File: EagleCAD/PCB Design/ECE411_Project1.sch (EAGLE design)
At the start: 23 parts

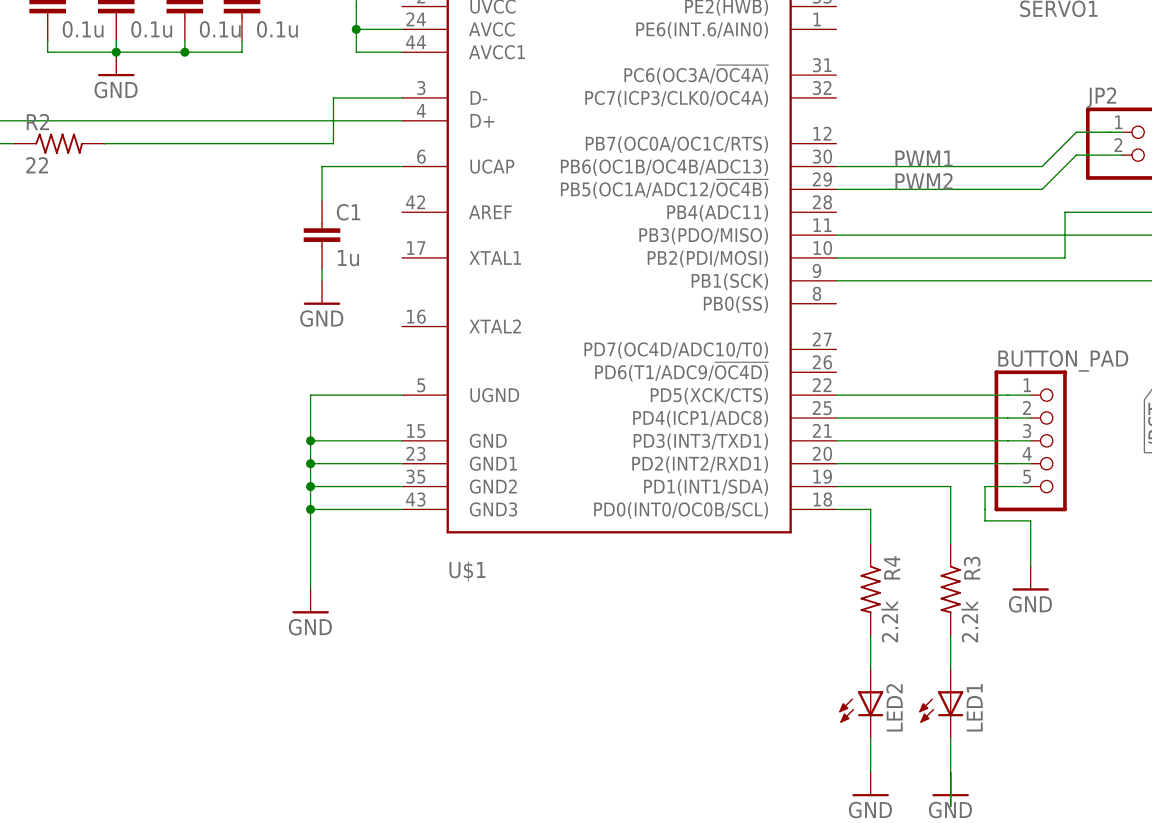
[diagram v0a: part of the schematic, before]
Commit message: Made Xtal library file
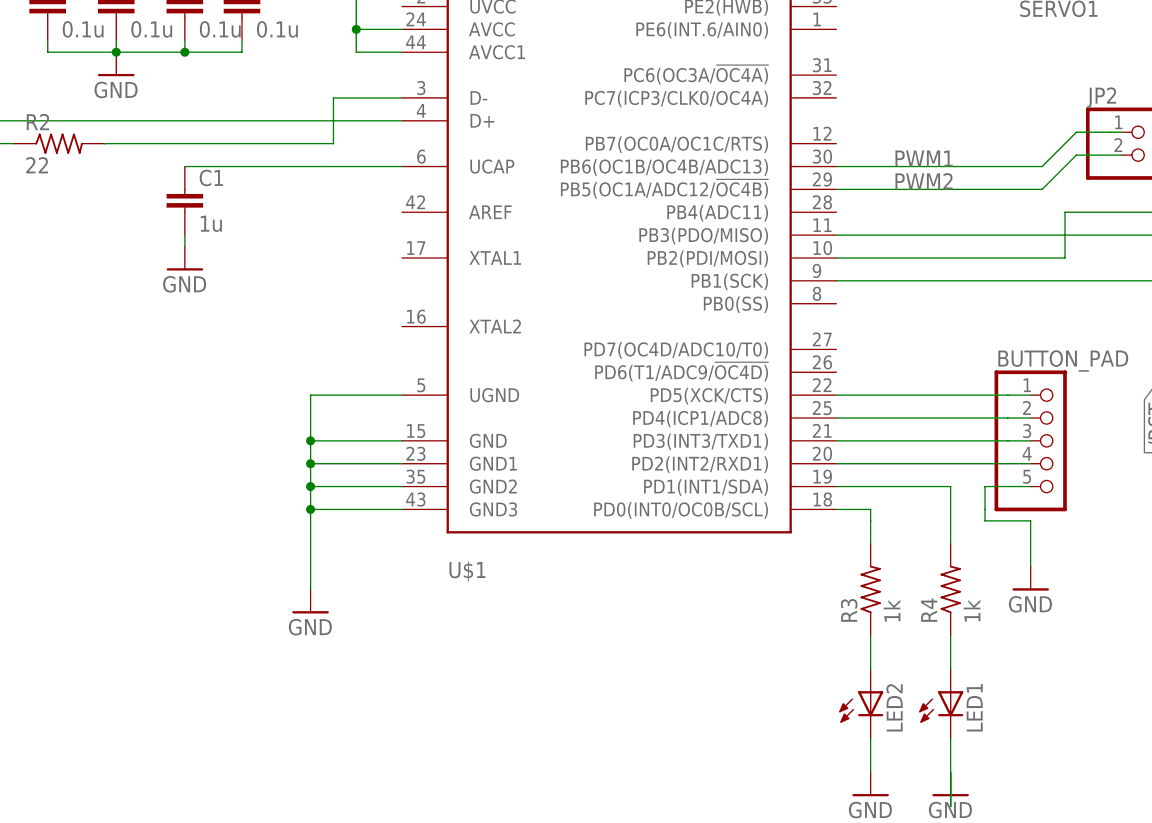
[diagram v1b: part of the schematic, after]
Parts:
- LED1, LED2: device adafruit:LED -> led:LEDSMT1206
- R3, R4: value (none) -> 1k; device rcl:R-US_0204/2V -> rcl:R-US_R1206; SPICEPREFIX 2.2k -> (none)
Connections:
- net N$10: now also R4.1; no longer R3.2
- net N$6: now also R3.2; no longer R4.1
- net N$8: now also R4.2; no longer R3.1
- net N$9: now also R3.1; no longer R4.2
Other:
- moved on the sheet: C1, R3, R4
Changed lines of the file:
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@@
 <part name="+3V1" library="supply1" library_urn="urn:adsk.eagle:library:371" deviceset="+3V3" device=""/>
 <part name="GND2" library="supply1" library_urn="urn:adsk.eagle:library:371" deviceset="GND" device=""/>
-<part name="LED1" library="adafruit" deviceset="LED" device=""/>
-<part name="R3" library="rcl" library_urn="urn:adsk.eagle:library:334" deviceset="R-US_" device="0204/2V" package3d_urn="urn:adsk.eagle:package:23495/1">
-<spice>
-<pinmapping spiceprefix="R">
-<pinmap gate="G$1" pin="1" pinorder="1"/>
-<pinmap gate="G$1" pin="2" pinorder="2"/>
-</pinmapping>
-</spice>
-<attribute name="SPICEPREFIX" value="2.2k"/>
-</part>
-<part name="R4" library="rcl" library_urn="urn:adsk.eagle:library:334" deviceset="R-US_" device="0204/2V" package3d_urn="urn:adsk.eagle:package:23495/1">
-<spice>
-<pinmapping spiceprefix="R">
-<pinmap gate="G$1" pin="1" pinorder="1"/>
-<pinmap gate="G$1" pin="2" pinorder="2"/>
-</pinmapping>
-</spice>
-<attribute name="SPICEPREFIX" value="2.2k"/>
-</part>
-<part name="LED2" library="adafruit" deviceset="LED" device=""/>
 <part name="GND3" library="supply1" library_urn="urn:adsk.eagle:library:371" deviceset="GND" device=""/>
 <part name="GND4" library="supply1" library_urn="urn:adsk.eagle:library:371" deviceset="GND" device=""/>
@@
 <part name="C1" library="rcl" library_urn="urn:adsk.eagle:library:334" deviceset="C-EU" device="C1206" package3d_urn="urn:adsk.eagle:package:23618/2" value="1u"/>
 <part name="R5" library="rcl" library_urn="urn:adsk.eagle:library:334" deviceset="R-US_" device="R1206" package3d_urn="urn:adsk.eagle:package:23540/2" value="10k"/>
+<part name="R3" library="rcl" library_urn="urn:adsk.eagle:library:334" deviceset="R-US_" device="R1206" package3d_urn="urn:adsk.eagle:package:23540/2" value="1k"/>
+<part name="R4" library="rcl" library_urn="urn:adsk.eagle:library:334" deviceset="R-US_" device="R1206" package3d_urn="urn:adsk.eagle:package:23540/2" value="1k"/>
+<part name="LED2" library="led" library_urn="urn:adsk.eagle:library:259" deviceset="LED" device="SMT1206" package3d_urn="urn:adsk.eagle:package:15796/1"/>
+<part name="LED1" library="led" library_urn="urn:adsk.eagle:library:259" deviceset="LED" device="SMT1206" package3d_urn="urn:adsk.eagle:package:15796/1"/>
 </parts>
 <sheets>
@@
 <instance part="MICRO_USB_TYPE_B" gate="G$1" x="-96.52" y="50.8"/>
 <instance part="+3V1" gate="G$1" x="-60.96" y="83.82"/>
-<instance part="GND2" gate="1" x="-30.48" y="33.02"/>
-<instance part="LED1" gate="G$1" x="39.37" y="-10.16">
-<attribute name="VALUE" x="45.085" y="-14.732" size="1.778" layer="96" rot="R90"/>
-</instance>
-<instance part="R3" gate="G$1" x="39.37" y="1.27" rot="R270">
-<attribute name="VALUE" x="36.068" y="5.08" size="1.778" layer="96" rot="R270"/>
-<attribute name="SPICEPREFIX" x="40.64" y="0" size="1.778" layer="96" rot="R270"/>
-</instance>
-<instance part="R4" gate="G$1" x="30.48" y="1.27" rot="R270">
-<attribute name="VALUE" x="27.178" y="5.08" size="1.778" layer="96" rot="R270"/>
-<attribute name="SPICEPREFIX" x="31.75" y="0" size="1.778" layer="96" rot="R270"/>
-</instance>
-<instance part="LED2" gate="G$1" x="30.48" y="-10.16">
-<attribute name="VALUE" x="36.195" y="-14.732" size="1.778" layer="96" rot="R90"/>
-</instance>
+<instance part="GND2" gate="1" x="-45.72" y="36.83"/>
 <instance part="GND3" gate="1" x="30.48" y="-21.59"/>
 <instance part="GND4" gate="1" x="39.37" y="-21.59"/>
@@
 <instance part="R1" gate="G$1" x="-72.39" y="53.34"/>
 <instance part="R2" gate="G$1" x="-59.69" y="50.8"/>
-<instance part="C1" gate="G$1" x="-30.48" y="41.91"/>
+<instance part="C1" gate="G$1" x="-45.72" y="45.72"/>
 <instance part="R5" gate="G$1" x="-27.94" y="92.71" rot="R90"/>
+<instance part="R3" gate="G$1" x="30.48" y="1.27" rot="R90"/>
+<instance part="R4" gate="G$1" x="39.37" y="1.27" rot="R90"/>
+<instance part="LED2" gate="G$1" x="30.48" y="-10.16"/>
+<instance part="LED1" gate="G$1" x="39.37" y="-10.16"/>
 </instances>
 <busses>
@@
 <segment>
 <pinref part="GND2" gate="1" pin="GND"/>
-<wire x1="-30.48" y1="36.83" x2="-30.48" y2="35.56" width="0.1524" layer="91"/>
+<wire x1="-45.72" y1="40.64" x2="-45.72" y2="39.37" width="0.1524" layer="91"/>
 <pinref part="C1" gate="G$1" pin="2"/>
 </segment>
 <segment>
-<pinref part="LED2" gate="G$1" pin="C"/>
 <wire x1="30.48" y1="-15.24" x2="30.48" y2="-19.05" width="0.1524" layer="91"/>
 <pinref part="GND3" gate="1" pin="GND"/>
-</segment>
-<segment>
-<pinref part="LED1" gate="G$1" pin="C"/>
+<pinref part="LED2" gate="G$1" pin="C"/>
+</segment>
+<segment>
 <wire x1="39.37" y1="-15.24" x2="39.37" y2="-22.86" width="0.1524" layer="91"/>
 <wire x1="39.37" y1="-22.86" x2="39.37" y2="-19.05" width="0.1524" layer="91"/>
 <pinref part="GND4" gate="1" pin="GND"/>
+<pinref part="LED1" gate="G$1" pin="C"/>
 </segment>
 <segment>
@@
 <pinref part="U$1" gate="G$1" pin="UCAP"/>
 <wire x1="-21.59" y1="48.26" x2="-30.48" y2="48.26" width="0.1524" layer="91"/>
-<wire x1="-30.48" y1="48.26" x2="-30.48" y2="44.45" width="0.1524" layer="91"/>
+<wire x1="-30.48" y1="48.26" x2="-45.72" y2="48.26" width="0.1524" layer="91"/>
 <pinref part="C1" gate="G$1" pin="1"/>
 </segment>
@@
 <wire x1="26.67" y1="10.16" x2="30.48" y2="10.16" width="0.1524" layer="91"/>
 <wire x1="30.48" y1="10.16" x2="30.48" y2="8.89" width="0.1524" layer="91"/>
+<wire x1="30.48" y1="8.89" x2="30.48" y2="6.35" width="0.1524" layer="91"/>
+<pinref part="R3" gate="G$1" pin="2"/>
+</segment>
+</net>
+<net name="N$9" class="0">
+<segment>
+<wire x1="30.48" y1="-3.81" x2="30.48" y2="-7.62" width="0.1524" layer="91"/>
+<pinref part="R3" gate="G$1" pin="1"/>
+<pinref part="LED2" gate="G$1" pin="A"/>
+</segment>
+</net>
+<net name="N$10" class="0">
+<segment>
+<wire x1="39.37" y1="-3.81" x2="39.37" y2="-7.62" width="0.1524" layer="91"/>
 <pinref part="R4" gate="G$1" pin="1"/>
-<wire x1="30.48" y1="8.89" x2="30.48" y2="6.35" width="0.1524" layer="91"/>
-</segment>
-</net>
-<net name="N$9" class="0">
-<segment>
-<pinref part="R4" gate="G$1" pin="2"/>
-<pinref part="LED2" gate="G$1" pin="A"/>
-<wire x1="30.48" y1="-3.81" x2="30.48" y2="-7.62" width="0.1524" layer="91"/>
-</segment>
-</net>
-<net name="N$10" class="0">
-<segment>
-<pinref part="R3" gate="G$1" pin="2"/>
 <pinref part="LED1" gate="G$1" pin="A"/>
-<wire x1="39.37" y1="-3.81" x2="39.37" y2="-7.62" width="0.1524" layer="91"/>
 </segment>
 </net>
@@
 <net name="N$8" class="0">
 <segment>
-<pinref part="R3" gate="G$1" pin="1"/>
 <wire x1="39.37" y1="6.35" x2="39.37" y2="12.7" width="0.1524" layer="91"/>
 <pinref part="U$1" gate="G$1" pin="PD1(INT1/SDA)"/>
 <wire x1="39.37" y1="12.7" x2="26.67" y2="12.7" width="0.1524" layer="91"/>
-</segment>
-</net>
+<pinref part="R4" gate="G$1" pin="2"/>
+</segment>
+</net>

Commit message: updates to schematic
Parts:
- removed 5V1A_REGULATOR1, 5V1A_REGULATOR2: L7805ABV, L7805ABV:L7805ABV
- added 16MHZ: XTAL_ATS160SM-1, XTAL_ATS160SM-1:XTAL_ATS160SM-1
- added C6, C7: 12p, rcl:C-EUC1206
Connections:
- removed net +3V3: C2.1, C3.1, C4.1, C5.1, U$1.AVCC, U$1.AVCC1, U$1.VCC, U$1.VCC1
- new net N$20: 16MHZ.2, C7.2, U$1.XTAL2
- new net N$21: 16MHZ.1, C6.2, U$1.XTAL1
- net GND: now also C2.1, C3.1, C4.1, C5.1, C6.1, C7.1; no longer 5V1A_REGULATOR1.GND, 5V1A_REGULATOR2.GND, C2.2, C3.2, C4.2, C5.2
- net N$14: no longer 5V1A_REGULATOR1.VOUT
- net N$19: no longer 5V1A_REGULATOR2.VOUT
- net VCC: now also C2.2, C3.2, C4.2, C5.2, U$1.AVCC, U$1.AVCC1, U$1.VCC, U$1.VCC1
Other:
- moved on the sheet: C2, C3, C4, C5

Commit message: Added some custom library components, updated schematic with new xtal cap values, and updated links document
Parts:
- removed JP2: (no value), pinhead:PINHD-1X2
- C6, C7: value 12p -> 22p
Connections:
- net PWM1: now also SERVO1.1; no longer JP2.1
- net PWM2: now also SERVO2.1; no longer JP2.2
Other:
- moved on the sheet: SERVO1, SERVO2
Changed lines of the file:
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@@
 <part name="BUTTON_PAD" library="pinhead" library_urn="urn:adsk.eagle:library:325" deviceset="PINHD-1X5" device="" package3d_urn="urn:adsk.eagle:package:22469/2"/>
 <part name="GND11" library="supply1" library_urn="urn:adsk.eagle:library:371" deviceset="GND" device=""/>
-<part name="JP2" library="pinhead" library_urn="urn:adsk.eagle:library:325" deviceset="PINHD-1X2" device="" package3d_urn="urn:adsk.eagle:package:22435/2"/>
 <part name="GND12" library="supply1" library_urn="urn:adsk.eagle:library:371" deviceset="GND" device=""/>
 <part name="GND13" library="supply1" library_urn="urn:adsk.eagle:library:371" deviceset="GND" device=""/>
@@
 <part name="LED2" library="led" library_urn="urn:adsk.eagle:library:259" deviceset="LED" device="SMT1206" package3d_urn="urn:adsk.eagle:package:15796/1"/>
 <part name="LED1" library="led" library_urn="urn:adsk.eagle:library:259" deviceset="LED" device="SMT1206" package3d_urn="urn:adsk.eagle:package:15796/1"/>
-<part name="C6" library="rcl" library_urn="urn:adsk.eagle:library:334" deviceset="C-EU" device="C1206" package3d_urn="urn:adsk.eagle:package:23618/2" value="12p"/>
-<part name="C7" library="rcl" library_urn="urn:adsk.eagle:library:334" deviceset="C-EU" device="C1206" package3d_urn="urn:adsk.eagle:package:23618/2" value="12p"/>
+<part name="C6" library="rcl" library_urn="urn:adsk.eagle:library:334" deviceset="C-EU" device="C1206" package3d_urn="urn:adsk.eagle:package:23618/2" value="22p"/>
+<part name="C7" library="rcl" library_urn="urn:adsk.eagle:library:334" deviceset="C-EU" device="C1206" package3d_urn="urn:adsk.eagle:package:23618/2" value="22p"/>
 <part name="GND14" library="supply1" library_urn="urn:adsk.eagle:library:371" deviceset="GND" device=""/>
 <part name="16MHZ" library="XTAL_ATS160SM-1" deviceset="XTAL_ATS160SM-1" device=""/>
@@
 <instance part="GND3" gate="1" x="30.48" y="-21.59"/>
 <instance part="GND4" gate="1" x="39.37" y="-21.59"/>
-<instance part="SERVO1" gate="A" x="49.53" y="72.39" rot="R180">
-<attribute name="VALUE" x="55.88" y="80.01" size="1.778" layer="96" rot="R180"/>
-</instance>
-<instance part="GND5" gate="1" x="71.12" y="72.39">
-<attribute name="VALUE" x="68.58" y="69.85" size="1.778" layer="96"/>
-</instance>
-<instance part="SERVO2" gate="A" x="85.09" y="72.39" rot="R180">
-<attribute name="VALUE" x="91.44" y="80.01" size="1.778" layer="96" rot="R180"/>
-</instance>
-<instance part="GND6" gate="1" x="107.95" y="72.39">
-<attribute name="VALUE" x="105.41" y="69.85" size="1.778" layer="96"/>
+<instance part="SERVO1" gate="A" x="52.07" y="73.66" rot="R90">
+<attribute name="VALUE" x="59.69" y="67.31" size="1.778" layer="96" rot="R90"/>
+</instance>
+<instance part="GND5" gate="1" x="54.61" y="63.5">
+<attribute name="VALUE" x="52.07" y="60.96" size="1.778" layer="96"/>
+</instance>
+<instance part="SERVO2" gate="A" x="71.12" y="73.66" rot="R90">
+<attribute name="VALUE" x="78.74" y="67.31" size="1.778" layer="96" rot="R90"/>
+</instance>
+<instance part="GND6" gate="1" x="73.66" y="63.5">
+<attribute name="VALUE" x="71.12" y="60.96" size="1.778" layer="96"/>
 </instance>
 <instance part="FRAME1" gate="G$1" x="-177.8" y="-76.2">
@@
 <attribute name="VALUE" x="45.72" y="-1.27" size="1.778" layer="96"/>
 </instance>
-<instance part="JP2" gate="G$1" x="60.96" y="49.53"/>
 <instance part="GND12" gate="1" x="-85.09" y="39.37"/>
 <instance part="GND13" gate="1" x="-66.04" y="57.15"/>
@@
 <segment>
 <pinref part="SERVO2" gate="A" pin="3"/>
-<wire x1="87.63" y1="74.93" x2="93.98" y2="74.93" width="0.1524" layer="91"/>
+<wire x1="73.66" y1="71.12" x2="73.66" y2="66.04" width="0.1524" layer="91"/>
 <pinref part="GND6" gate="1" pin="GND"/>
-<wire x1="93.98" y1="74.93" x2="107.95" y2="74.93" width="0.1524" layer="91"/>
 </segment>
 <segment>
@@
 <pinref part="GND5" gate="1" pin="GND"/>
 <pinref part="SERVO1" gate="A" pin="3"/>
-<wire x1="71.12" y1="74.93" x2="52.07" y2="74.93" width="0.1524" layer="91"/>
+<wire x1="54.61" y1="66.04" x2="54.61" y2="71.12" width="0.1524" layer="91"/>
 </segment>
 <segment>
@@
 <wire x1="26.67" y1="45.72" x2="49.53" y2="45.72" width="0.1524" layer="91"/>
 <label x="33.02" y="45.72" size="1.778" layer="95"/>
-<pinref part="JP2" gate="G$1" pin="2"/>
-<wire x1="58.42" y1="49.53" x2="53.34" y2="49.53" width="0.1524" layer="91"/>
-<wire x1="53.34" y1="49.53" x2="49.53" y2="45.72" width="0.1524" layer="91"/>
+<pinref part="SERVO2" gate="A" pin="1"/>
+<wire x1="49.53" y1="45.72" x2="68.58" y2="45.72" width="0.1524" layer="91"/>
+<wire x1="68.58" y1="45.72" x2="68.58" y2="71.12" width="0.1524" layer="91"/>
 </segment>
 </net>
@@
 <wire x1="26.67" y1="48.26" x2="49.53" y2="48.26" width="0.1524" layer="91"/>
 <label x="33.02" y="48.26" size="1.778" layer="95"/>
-<wire x1="49.53" y1="48.26" x2="53.34" y2="52.07" width="0.1524" layer="91"/>
-<wire x1="53.34" y1="52.07" x2="57.15" y2="52.07" width="0.1524" layer="91"/>
-<pinref part="JP2" gate="G$1" pin="1"/>
-<wire x1="57.15" y1="52.07" x2="58.42" y2="52.07" width="0.1524" layer="91"/>
+<pinref part="SERVO1" gate="A" pin="1"/>
+<wire x1="49.53" y1="71.12" x2="49.53" y2="48.26" width="0.1524" layer="91"/>
 </segment>
 </net>
@@
 <segment>
 <pinref part="SERVO1" gate="A" pin="2"/>
-<wire x1="52.07" y1="72.39" x2="66.04" y2="72.39" width="0.1524" layer="91"/>
+<wire x1="52.07" y1="71.12" x2="52.07" y2="58.42" width="0.1524" layer="91"/>
 </segment>
 </net>
@@
 <segment>
 <pinref part="SERVO2" gate="A" pin="2"/>
-<wire x1="87.63" y1="72.39" x2="101.6" y2="72.39" width="0.1524" layer="91"/>
-</segment>
-</net>
+<wire x1="71.12" y1="71.12" x2="71.12" y2="58.42" width="0.1524" layer="91"/>
+</segment>
+</net>

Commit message: Updated Schematic
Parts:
- removed 16MHZ: XTAL_ATS160SM-1, XTAL_ATS160SM-1:XTAL_ATS160SM-1
- removed JP1: (no value), pinhead:PINHD-2X3
- removed MICRO_USB_TYPE_B: USB-A, adafruit:USB-A
- removed S1: SPST, adafruit:SPST
- added ISP1: AVRISP-6, USB_Micro_and_AVRISP:AVRISP-6
- added J1: 0473460001_USBMICRO, USB_Micro_and_AVRISP:0473460001_USBMICRO
- added SW1: FSM2JSMLTR, Push_Button:FSM2JSMLTR
- added U1: ATS160SM-1, Xtals:ATS160SM-1
- added U2: MIC29310-5.0WU, Regulators:MIC29310-5.0WU
- added U3: NCP5501DT50RKG, Regulators:NCP5501DT50RKG
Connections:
- removed net DC_PWR_5V_2A: CN1.PWR
- removed net N$14: SERVO1.2
- removed net N$19: SERVO2.2
- new net N$22: CN1.PWR, U2.IN, U3.IN
- new net SERVO_PWR: SERVO1.2, SERVO2.2, U2.OUT
- net /RST: now also ISP1.RST, SW1.1, SW1.3; no longer JP1.5, S1.S
- net GND: now also CN1.GND, CN1.GNDBREAK, ISP1.GND, J1.GND, SW1.2, SW1.4, U2.GND, U3.GND; no longer JP1.6, MICRO_USB_TYPE_B.GND, S1.P
- net N$1: now also J1.D+; no longer MICRO_USB_TYPE_B.D+
- net N$15: now also ISP1.VCC; no longer JP1.2
- net N$16: now also ISP1.MISO; no longer JP1.1
- net N$17: now also ISP1.MOSI; no longer JP1.4
- net N$18: now also ISP1.SCK; no longer JP1.3
- net N$20: now also U1.1; no longer 16MHZ.2
- net N$21: now also U1.2; no longer 16MHZ.1
- net N$3: now also J1.D-; no longer MICRO_USB_TYPE_B.D-
- net VCC: now also U3.OUT
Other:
- moved on the sheet: CN1
